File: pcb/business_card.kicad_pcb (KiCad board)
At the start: 16 copper layers, 88.9 x 50.8 mm, 71 parts, among them J3 USB_A, J4 Conn_ARM_SWD_TagConnect_TC2030, SW1 SW_SPST, U1 MIC5504-3.3YM5, U2 STM32G030F6P6

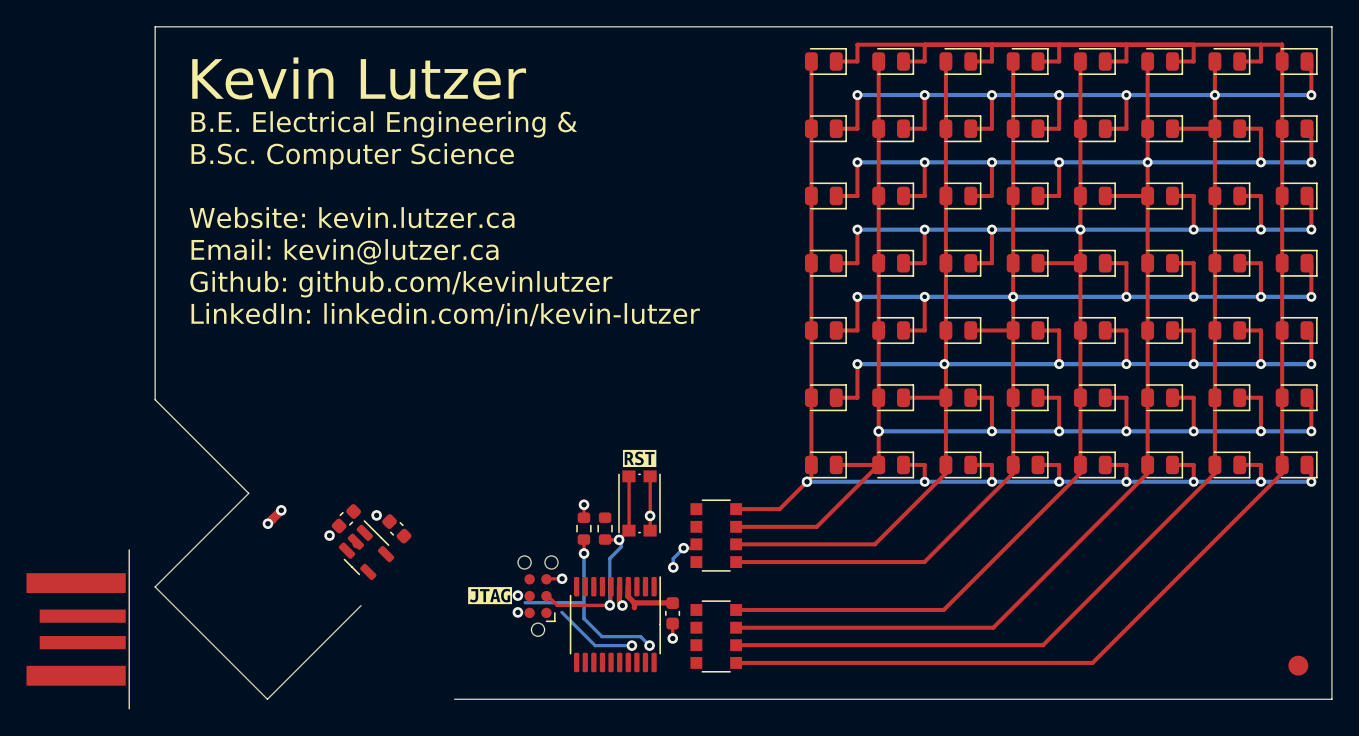
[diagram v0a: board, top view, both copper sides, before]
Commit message: remove the progremmwer and the eagle files, rename everything to just business card
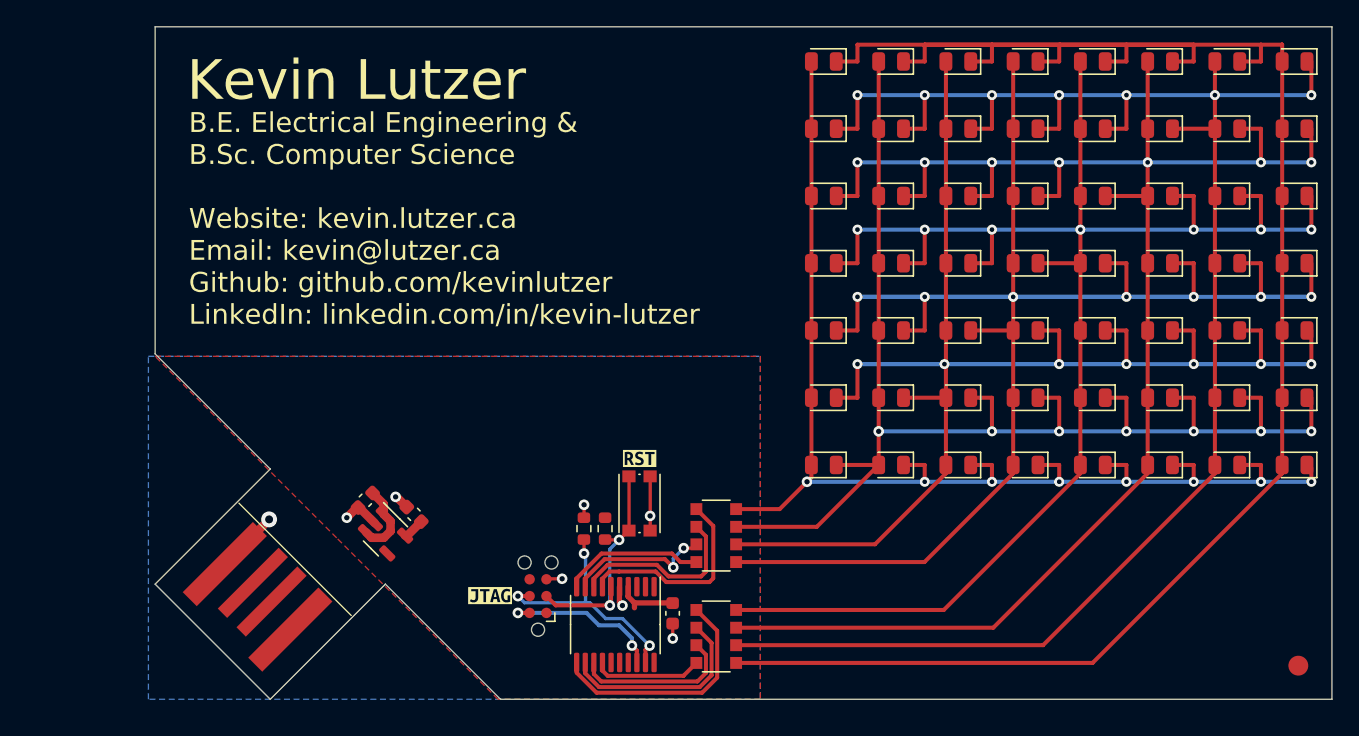
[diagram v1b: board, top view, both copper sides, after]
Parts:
- LED1, LED2: value LEDCHIPLED_0805 -> LED
- moved J3 13.9 mm to (106.9, 121.7), turned to 45 degrees
- moved C4 2.00 mm to (114.9, 114.5)
- moved U1 2.00 mm to (116.5, 117.0)
- moved C2 1.70 mm to (118.6, 115.6)
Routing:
- net PINE: track 0.00 -> 18.2 mm
- net PINA: track 0.00 -> 15.4 mm
- net PINF: track 0.00 -> 15.2 mm
- net PINB: track 0.00 -> 13.7 mm
- net PING: track 0.00 -> 12.2 mm
- net PIND: track 0.00 -> 10.7 mm
- net PINH: track 0.00 -> 8.28 mm
- net PINC: track 2.96 -> 11.1 mm
- net GND: track 9.85 -> 17.8 mm, vias 9 -> 8
- net SWDIO: track 6.33 -> 12.3 mm
- net +5V: track 0.00 -> 5.68 mm
- net SWDCLK: track 16.3 -> 18.6 mm
- net +3V3: track 4.69 -> 6.36 mm
- added copper zone on F.Cu, net +3V3
- added copper zone on B.Cu, net GND
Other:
- outline, holes or cut-outs redrawn
- copper layers 16 -> 2
